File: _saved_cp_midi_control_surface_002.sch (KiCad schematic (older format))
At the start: 23 parts, among them P1 Power, P2 Analogue, P3 Digital, P4 Communication, P5 PWM, P6 PWM

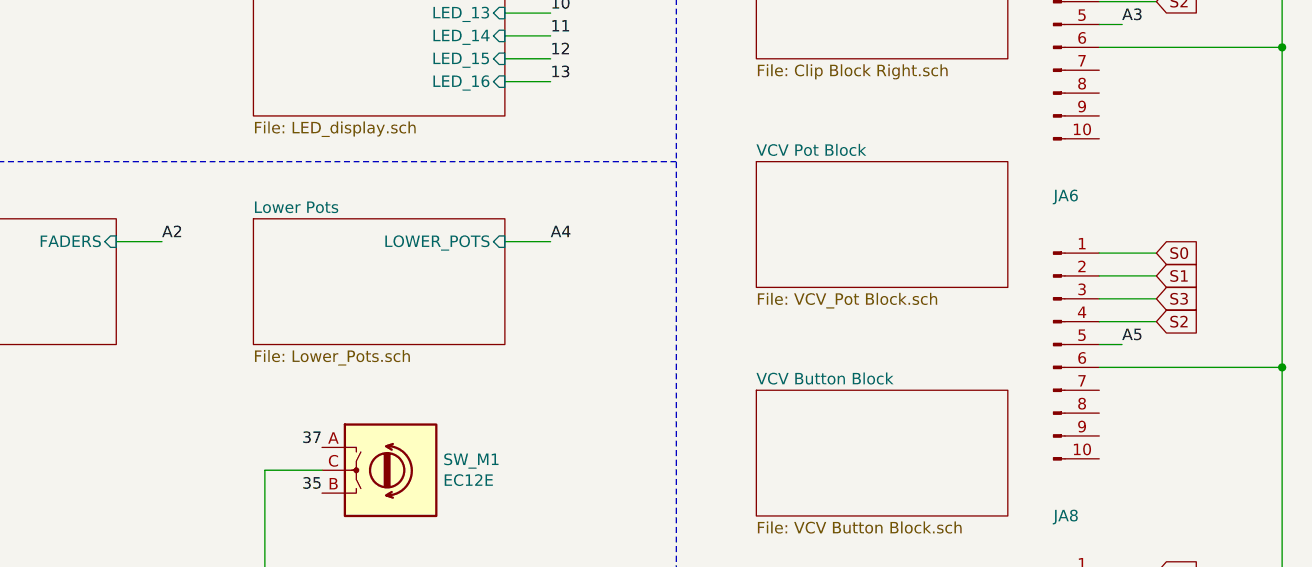
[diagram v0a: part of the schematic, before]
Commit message: Reordered COM contacts and added initial trace positions
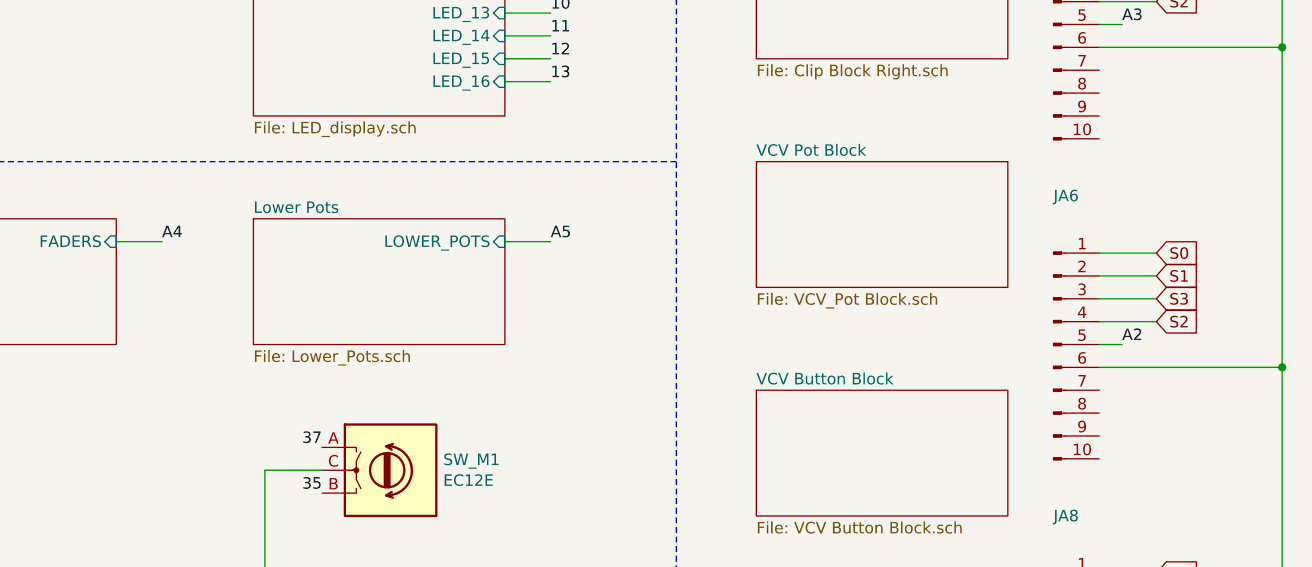
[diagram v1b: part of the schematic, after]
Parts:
- P2: footprint Connector_PinHeader_2.54mm:PinHeader_1x06_P2.54mm_Vertical -> Connector_PinHeader_2.54mm:PinHeader_1x08_P2.54mm_Vertical
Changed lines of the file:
@@
 F 0 "P2" H 9250 3650 50  0000 C CNN
 F 1 "Analogue" V 9350 3250 50  0000 C CNN
-F 2 "Connector_PinHeader_2.54mm:PinHeader_1x06_P2.54mm_Vertical" H 9250 3250 50  0001 C CNN
+F 2 "Connector_PinHeader_2.54mm:PinHeader_1x08_P2.54mm_Vertical" H 9250 3250 50  0001 C CNN
 F 3 "" H 9250 3250 50  0000 C CNN
 	1    9250 3250
@@
 $EndSheet
 Text Label 3950 3600 0    50   ~ 0
-A4
+A5
 Wire Wire Line
 	3750 3600 3950 3600
@@
 $EndComp
 Text Label 6450 4050 0    50   ~ 0
-A5
+A2
 $Comp
 L Connector:Conn_01x10_Male JA6
@@
 	10500 5750 10500 5550
 Text Label 2250 3600 0    50   ~ 0
-A2
+A4
 Wire Wire Line
 	2050 3600 2250 3600
